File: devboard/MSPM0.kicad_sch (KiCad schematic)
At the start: 24 parts, among them J1 USB_C_USB2.0, SW1 SW, SW2 SW_Push, U1 MSPM0G3507SPMR, U2 AP2112K-3.3, U3 CH340C

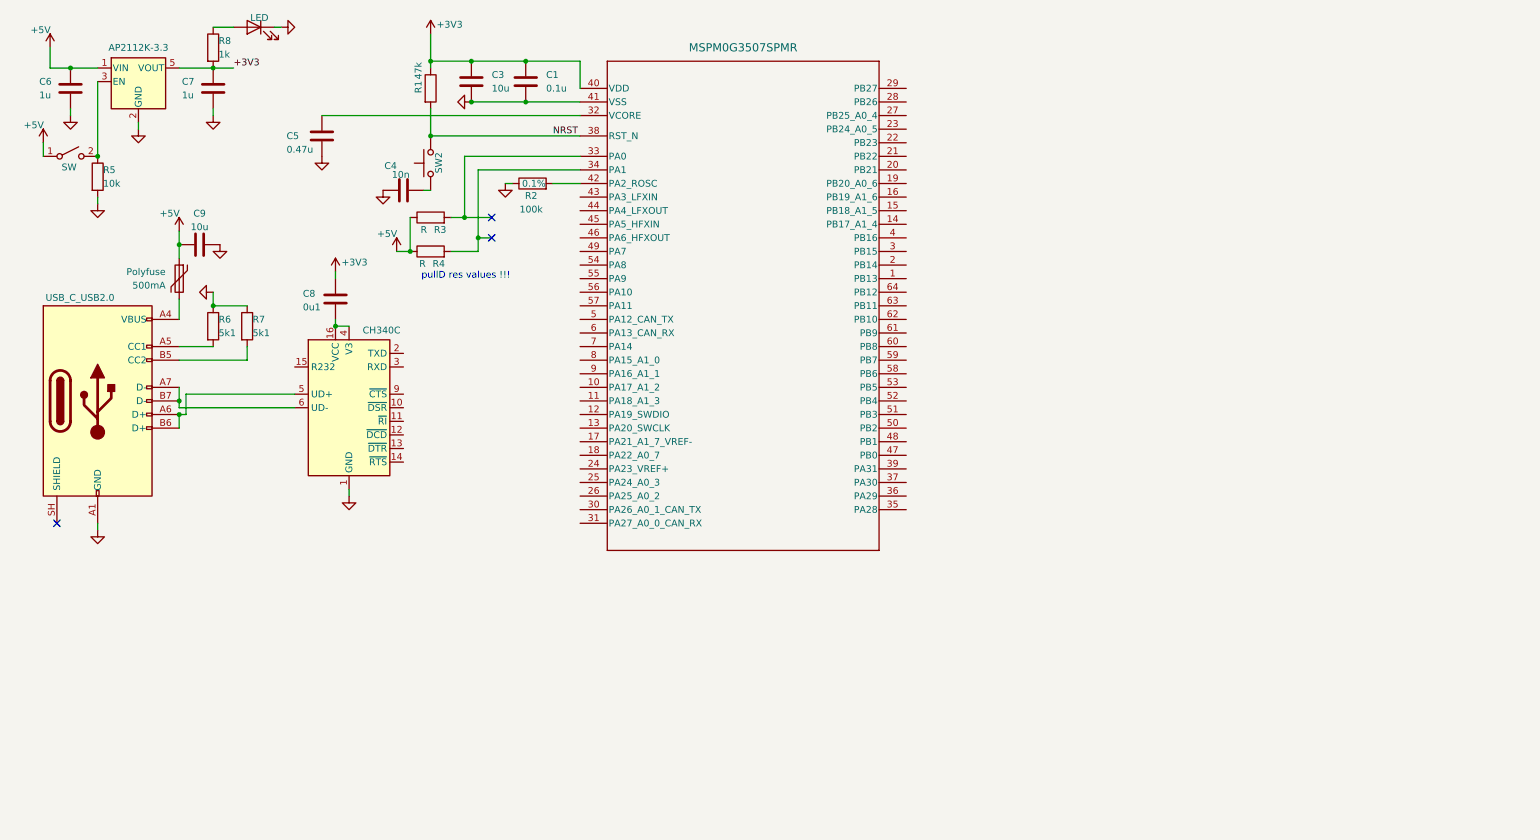
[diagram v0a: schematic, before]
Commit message: added SWD header and configured USB-UART a bit
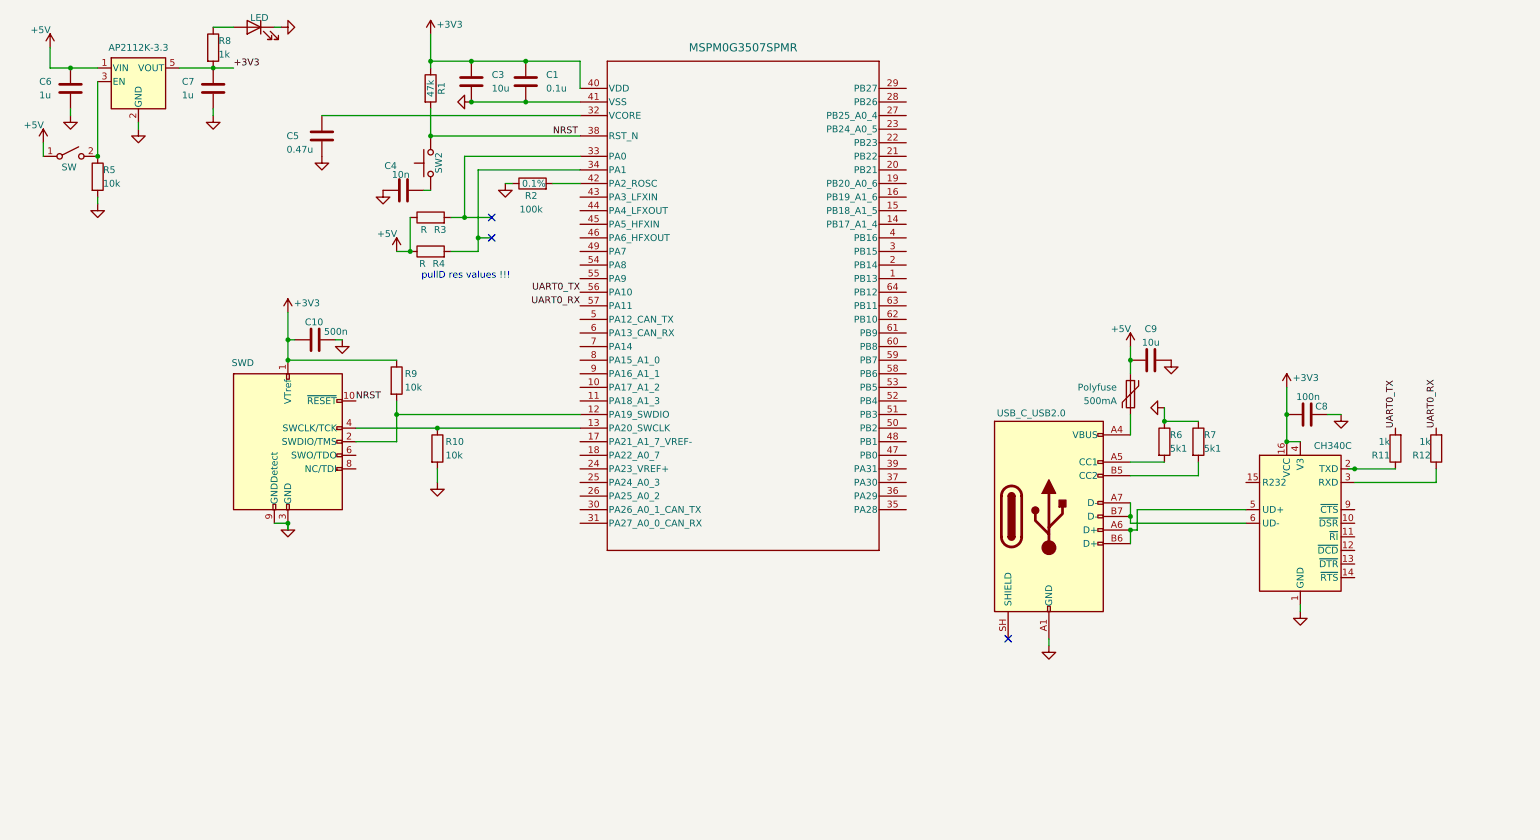
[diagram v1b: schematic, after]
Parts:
- added C10: 500n, symbol Device:C
- added J2: SWD, symbol Connector:Conn_ARM_JTAG_SWD_10
- added R10, R9: 10k, symbol Device:R
- added R11, R12: 1k, symbol Device:R
- C8: value 0u1 -> 100n
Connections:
- net +3V3: now also C8.2, U3.16 (VCC), U3.4 (V3), C10.1, J2.1 (VTref), R9.1; no longer C8.1
- net GND: now also C8.1, C10.2, J2.3 (GND), J2.5 (GND), J2.9 (GNDDetect), R10.2
- net NRST: now also J2.10 (~{RESET})
- net at U1.12 (PA19_SWDIO): now also J2.2 (SWDIO/TMS), R9.2
- net at U1.13 (PA20_SWCLK): now also J2.4 (SWCLK/TCK), R10.1
- net UART0_TX: now reaches U1.56 (PA10)
- net UART0_TX: now also R11.2
- net UART0_RX: now reaches U1.57 (PA11)
- net UART0_RX: now also R12.2
- net at U3.2 (TXD): now also R11.1
- net at U3.3 (RXD): now also R12.1
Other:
- moved on the sheet: C9, Polyfuse, R6, R7

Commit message: gotta start CAN FD
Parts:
- added U4: TCAN1044AVDDFRQ1.A, DDF0008A-IPC_A, symbol TCAN1044AV:TCAN1044AVDDFRQ1.A
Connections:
- net SWO: now reaches U1.8 (PA15_A1_0)
- net SWO: now also J2.6 (SWO/TDO)
- no-connect marks 3 -> 4
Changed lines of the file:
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@@
 		(at 102.87 54.61)
 	)
+	(no_connect
+		(at 77.47 97.79)
+	)
 	(wire
 		(pts
@@
 		)
 	)
+	(label "SWO"
+		(at 119.38 77.47 180)
+		(effects
+			(font
+				(size 1.27 1.27)
+			)
+			(justify right bottom)
+		)
+	)
 	(label "UART0_RX"
 		(at 279.4 90.17 90)
@@
 		)
 	)
+	(label "SWO"
+		(at 77.47 95.25 0)
+		(effects
+			(font
+				(size 1.27 1.27)
+			)
+			(justify left bottom)
+		)
+	)
 	(label "NRST"
 		(at 114.3 35.56 0)
@@
 					(unit 1)
 				)
+			)
+		)
+	)
+	(symbol
+		(lib_id "TCAN1044AV:TCAN1044AVDDFRQ1.A")
+		(at 45.72 134.62 0)
+		(unit 1)
+		(body_style 1)
+		(exclude_from_sim no)
+		(in_bom yes)
+		(on_board yes)
+		(in_pos_files yes)
+		(dnp no)
+		(fields_autoplaced yes)
+		(property "Reference" "U4"
+			(at 66.04 124.46 0)
+			(hide yes)
+			(show_name no)
+			(do_not_autoplace no)
+			(effects
+				(font
+					(size 1.524 1.524)
+				)
+			)
+		)
+		(property "Value" "TCAN1044AVDDFRQ1.A"
+			(at 66.04 127 0)
+			(show_name no)
+			(do_not_autoplace no)
+			(effects
+				(font
+					(size 1.524 1.524)
+				)
+			)
+		)
+		(property "Footprint" "DDF0008A-IPC_A"
+			(at 45.72 134.62 0)
+			(hide yes)
+			(show_name no)
+			(do_not_autoplace no)
+			(effects
+				(font
+					(size 1.27 1.27)
+					(italic yes)
+				)
+			)
+		)
+		(property "Datasheet" "https://www.ti.com/lit/gpn/tcan1044a-q1"
+			(at 45.72 134.62 0)
+			(hide yes)
+			(show_name no)
+			(do_not_autoplace no)
+			(effects
+				(font
+					(size 1.27 1.27)
+					(italic yes)
+				)
+			)
+		)
+		(property "Description" ""
+			(at 45.72 134.62 0)
+			(hide yes)
+			(show_name no)
+			(do_not_autoplace no)
+			(effects
+				(font
+					(size 1.27 1.27)
+				)
+			)
+		)
+		(pin "1"
+		)
+		(pin "4"
+		)
+		(pin "2"
+		)
+		(pin "3"
+		)
+		(pin "6"
+		)
+		(pin "8"
+		)
+		(pin "7"
+		)
+		(pin "5"
+		)
+		(instances
+			(project "MSPM0"
+				(path "/3004d868-29f4-471c-a613-f1fb79301ae2"
+					(reference "U4")
+					(unit 1)
+				)

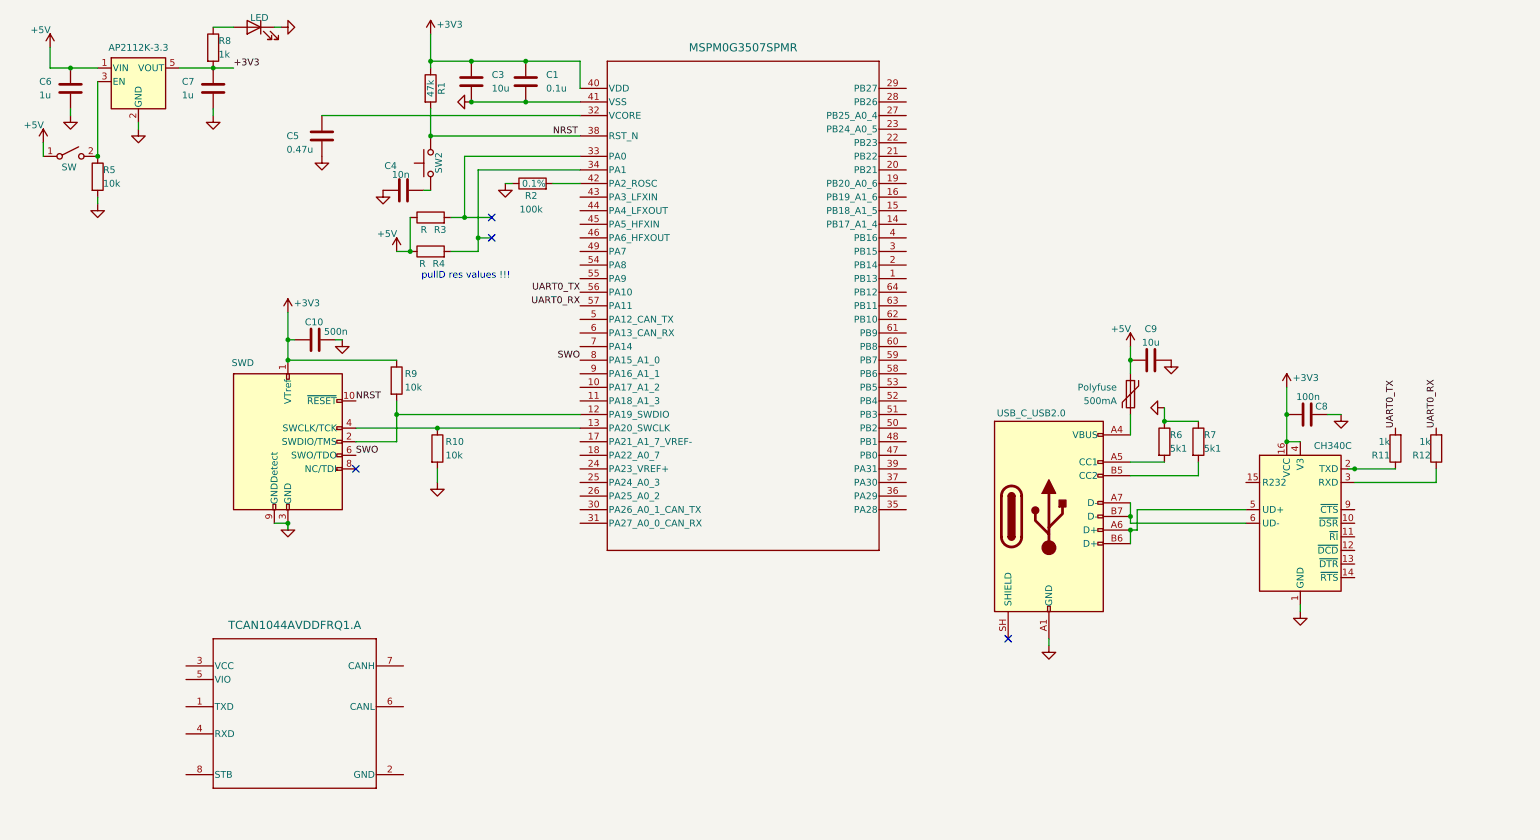
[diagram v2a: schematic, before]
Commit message: 2 LEDs, crystal, and some aesthetics
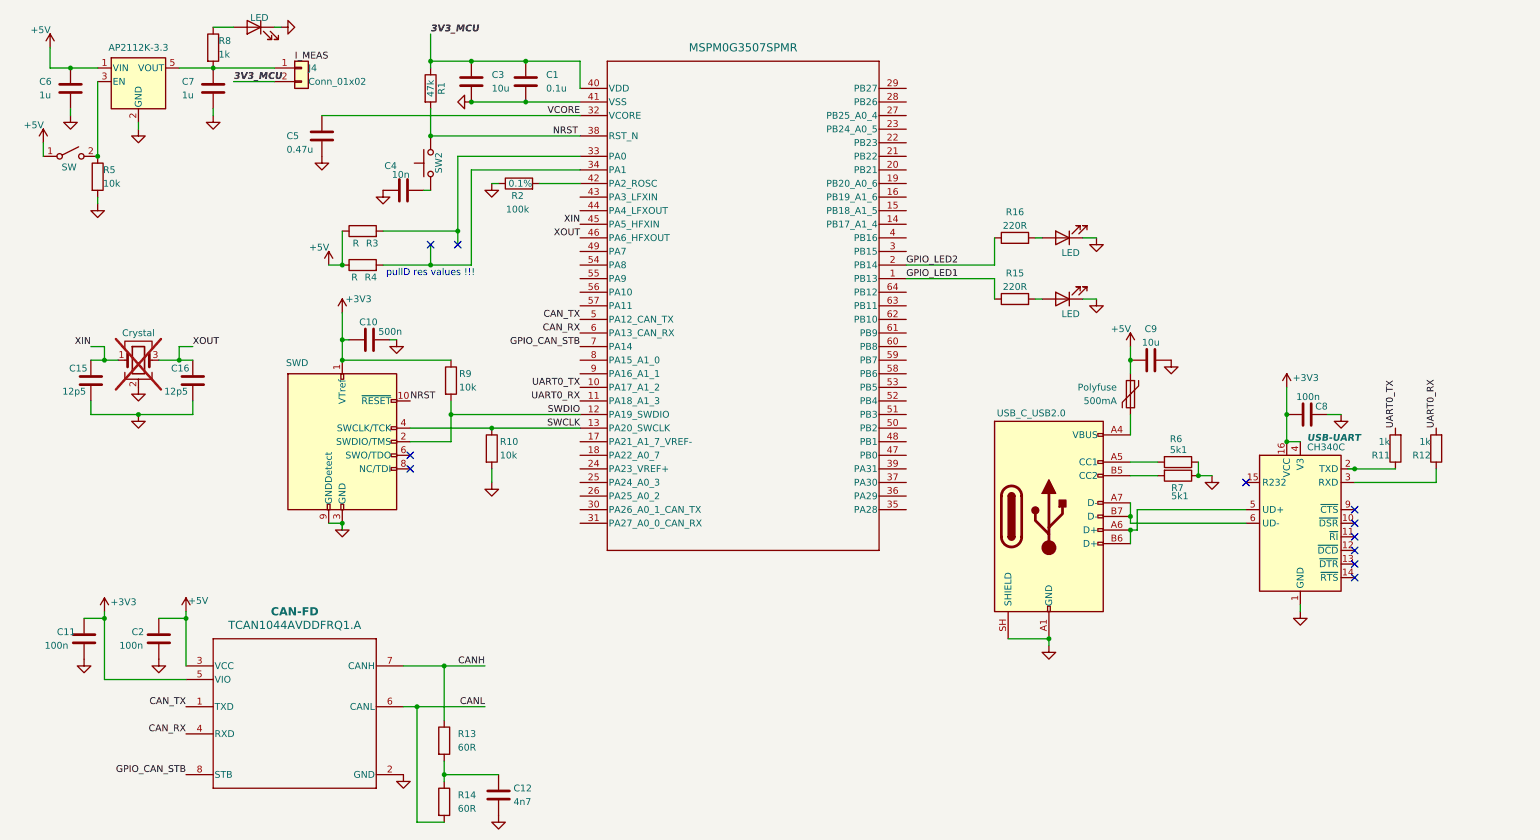
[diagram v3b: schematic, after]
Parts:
- added C11, C2: 100n, symbol Device:C
- added C12: 4n7, symbol Device:C
- added C15, C16: 12p5, symbol Device:C
- added D2, D3: LED, symbol Device:LED
- added J4: Conn_01x02, Connector_PinHeader_2.54mm:PinHeader_1x02_P2.54mm_Vertical, symbol Connector_Generic:Conn_01x02
- added R13, R14: 60R, symbol Device:R
- added R15, R16: 220R, symbol Device:R
- added Y1: Crystal, symbol Device:Crystal_GND24
- renumbered U4 to CAN-FD, U3 to USB-UART
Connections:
- net +3V3: now also CAN-FD.5 (VIO), C11.1; no longer C1.1, C3.1, C7.1, R1.1, R8.2, U1.40 (VDD), U2.5 (VOUT)
- net +5V: now also CAN-FD.3 (VCC), C2.1
- net GND: now also CAN-FD.2 (GND), J1.SH (SHIELD), C11.2, C12.2, C15.2, C16.2, C2.2, D2.1 (K), D3.1 (K), Y1.2 (G), Y1.4 (G)
- net UART0_RX: now also U1.11 (PA18_A1_3); no longer U1.57 (PA11)
- net UART0_TX: now also U1.10 (PA17_A1_2); no longer U1.56 (PA10)
- net SWCLK: now reaches J2.4 (SWCLK/TCK), R10.1, U1.13 (PA20_SWCLK)
- net GPIO_LED1: now reaches U1.1 (PB13)
- net GPIO_LED1: now also R15.1
- net SWDIO: now reaches J2.2 (SWDIO/TMS), R9.2, U1.12 (PA19_SWDIO)
- net GPIO_LED2: now reaches U1.2 (PB14)
- net GPIO_LED2: now also R16.1
- net VCORE: now reaches C5.1, U1.32 (VCORE)
- net XIN: now reaches U1.45 (PA5_HFXIN)
- net XIN: now also C15.1, Y1.1
- net XOUT: now reaches U1.46 (PA6_HFXOUT)
- net XOUT: now also C16.1, Y1.3
- net CAN_TX: now reaches U1.5 (PA12_CAN_TX)
- net CAN_TX: now also CAN-FD.1 (TXD)
- net CAN_RX: now reaches U1.6 (PA13_CAN_RX)
- net CAN_RX: now also CAN-FD.4 (RXD)
- net GPIO_CAN_STB: now reaches U1.7 (PA14)
- net GPIO_CAN_STB: now also CAN-FD.8 (STB)
- net CANL: now reaches CAN-FD.6 (CANL)
- net CANL: now also R14.2
- net CANH: now reaches CAN-FD.7 (CANH)
- net CANH: now also R13.1
- net SWO: no longer names the net of U1.8 (PA15_A1_0)
- net SWO: no longer J2.6 (SWO/TDO)
- new net: C7.1, J4.1 (Pin_1), R8.2, U2.5 (VOUT)
- new net: D2.2 (A), R15.2
- new net: C12.1, R13.2, R14.1
- new net: D3.2 (A), R16.2
- new net 3V3_MCU: C1.1, C3.1, J4.2 (Pin_2), R1.1, U1.40 (VDD)
- no-connect marks 4 -> 11
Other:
- moved on the sheet: C10, R10, R2, R3, R4, R6, R7, R9

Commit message: got rid of ERC errors
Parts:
- removed Y1: Crystal, symbol Device:Crystal_GND24
- added JP1: Jumper_2_Bridged, symbol Jumper:Jumper_2_Bridged
- added R17: 47k, symbol Device:R
- added SW3: SW, symbol Switch:SW_Push
- added TP1: TP_5V, symbol Connector:TestPoint
- added TP2: TP_3V3, symbol Connector:TestPoint
- added Y2: Crystal, Crystal:Crystal_SMD_3225-4Pin_3.2x2.5mm, symbol Device:Crystal_GND24
- C10: value 500n -> 470n
- C15, C16: value 12p5 -> 15p; now not fitted
- CAN-FD1: renamed from CAN-FD; footprint DDF0008A-IPC_A -> TCAN1044AV:DDF0008A-IPC_A
- MCU1: renamed from U1; footprint PM0064A-IPC_A -> MSPM0G3507SPMR (ft):PM0064A-IPC_A
- R13, R14: value 60R -> 62R
- R15, R16: value 220R -> 1k
- R3, R4: value R -> 4k7
- R5, SW1: now not fitted
- R8: value 1k -> 470R
- renumbered Polyfuse to Polyfuse1, USB-UART to USB-UART1
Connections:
- net +3V3: now also C7.1, J4.1 (Pin_1), R3.1, R4.1, R8.2, U2.5 (VOUT), TP2.1
- net +5V: now also C1.2, C10.2, C11.2, C12.2, C15.2, C16.2, C2.2, C3.2, C4.2, C5.2, C6.2, C7.2, C8.1, C9.2, CAN-FD1.2 (GND), D1.1 (K), D2.1 (K), D3.1 (K), J1.A1 (GND), J1.A12 (GND), J1.B1 (GND), J1.B12 (GND), J1.SH (SHIELD), J2.3 (GND), J2.5 (GND), J2.9 (GNDDetect), MCU1.41 (VSS), R10.2, R2.1, R6.1, R7.1, SW2.1, U2.2 (GND), U2.3 (EN), USB-UART1.1 (GND), R17.1, TP1.1, Y2.2 (G), Y2.4 (G); no longer R3.1, R4.1, SW1.1 (A)
- net CANH: now also JP1.1 (A); no longer R13.1
- net NRST: now also C4.1
- net UART0_RX: now also SW3.1
- net XIN: now also Y2.1
- net XOUT: now also Y2.3
- net I2C_SDA: now reaches MCU1.34 (PA1), R4.2
- net at R5.1, SW1.2 (B): no longer U2.3 (EN)
- net I2C_SCL: now reaches MCU1.33 (PA0), R3.2
- removed net GND: C1.2, C10.2, C11.2, C12.2, C15.2, C16.2, C2.2, C3.2, C4.2, C5.2, C6.2, C7.2, C8.1, C9.2, CAN-FD1.2 (GND), D1.1 (K), D2.1 (K), D3.1 (K), J1.A1 (GND), J1.A12 (GND), J1.B1 (GND), J1.B12 (GND), J1.SH (SHIELD), J2.3 (GND), J2.5 (GND), J2.9 (GNDDetect), MCU1.41 (VSS), R10.2, R2.1, R5.2, R6.1, R7.1, U2.2 (GND), USB-UART1.1 (GND)
- new net: R17.2, SW3.2
- new net: JP1.2 (B), R13.1
- no-connect marks 11 -> 57
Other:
- note removed: "pullD res values !!!"
- moved on the sheet: C10, R10, R9

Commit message: started the UNO headers
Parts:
- added J3, J5: Conn_01x03_Pin, symbol Connector:Conn_01x03_Pin
- added R18, R19: 10k, symbol Device:R
- added SW4, SW5: SW_Push, symbol Switch:SW_Push
- added TP3, TP4: TP_GND, symbol Connector:TestPoint
- added TP5: TP_SWDIO, symbol Connector:TestPoint
- added TP6: TP_SWDCLK, symbol Connector:TestPoint
- added TP7: TP_NRST, symbol Connector:TestPoint
- added TP8: TP_UART_RX, symbol Connector:TestPoint
- added TP9: TP_UART_TX, symbol Connector:TestPoint
- C15, C16: now fitted
- MCU1: value MSPM0G3507SPMR -> MSPM0G3507SPMR (LQFP-64)
- Y2: value Crystal -> 40MHz
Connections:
- net +5V: no longer C1.2, C10.2, C11.2, C12.2, C15.2, C16.2, C2.2, C3.2, C4.2, C5.2, C6.2, C7.2, C8.1, C9.2, CAN-FD1.2 (GND), D1.1 (K), D2.1 (K), D3.1 (K), J1.A1 (GND), J1.A12 (GND), J1.B1 (GND), J1.B12 (GND), J1.SH (SHIELD), J2.3 (GND), J2.5 (GND), J2.9 (GNDDetect), MCU1.41 (VSS), R10.2, R17.1, R2.1, R6.1, R7.1, SW2.1, U2.2 (GND), USB-UART1.1 (GND), Y2.2 (G), Y2.4 (G)
- net 3V3_MCU: now also R18.1, R19.1, TP4.1
- net CANH: now also J5.3 (Pin_3)
- net CANL: now also J5.2 (Pin_2)
- net NRST: now also TP7.1
- net SWCLK: now also TP6.1
- net SWDIO: now also TP5.1
- net UART0_RX: now also J3.2 (Pin_2), TP8.1
- net UART0_TX: now also J3.3 (Pin_3), TP9.1
- net PWM_0: now reaches MCU1.17 (PA21_A1_7_VREF-)
- net GPIO_Button1: now reaches MCU1.3 (PB15)
- net GPIO_Button1: now also R18.2, SW4.1
- net GPIO_Button2: now reaches MCU1.4 (PB16)
- net GPIO_Button2: now also R19.2, SW5.1
- net SPI_PICO: now reaches MCU1.55 (PA9)
- net SPI_POCI: now reaches MCU1.56 (PA10)
- net SPI_SCLK: now reaches MCU1.57 (PA11)
- new net GND: C1.2, C10.2, C11.2, C12.2, C15.2, C16.2, C2.2, C3.2, C4.2, C5.2, C6.2, C7.2, C8.1, C9.2, CAN-FD1.2 (GND), D1.1 (K), D2.1 (K), D3.1 (K), J1.A1 (GND), J1.A12 (GND), J1.B1 (GND), J1.B12 (GND), J1.SH (SHIELD), J2.3 (GND), J2.5 (GND), J2.9 (GNDDetect), J3.1 (Pin_1), J5.1 (Pin_1), MCU1.41 (VSS), R10.2, R17.1, R2.1, R6.1, R7.1, SW2.1, SW4.2, SW5.2, TP3.1, U2.2 (GND), USB-UART1.1 (GND), Y2.2 (G), Y2.4 (G)
- no-connect marks 57 -> 51
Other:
- moved on the sheet: R15, R16

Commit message: bro the faah is that pwm doing with ccp0/ccp1 😭
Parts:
- added J6: Conn_01x08_Power, symbol Connector:Conn_01x08_Socket
- added J7: Conn_01x06_Analog, symbol Connector:Conn_01x06_Socket
- added J8: Conn_01x08_DigitalLow, symbol Connector:Conn_01x08_Socket
- added J9: Conn_01x10_DigitalHigh, symbol Connector:Conn_01x10_Socket
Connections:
- net +5V: now also J6.5 (Pin_5)
- net 3V3_MCU: now also J6.4 (Pin_4)
- net GND: now also J6.6 (Pin_6), J6.7 (Pin_7)
- net GPIO_Button1: now also J8.6 (Pin_6)
- net GPIO_Button2: now also J8.7 (Pin_7)
- net GPIO_LED1: now also J8.3 (Pin_3)
- net GPIO_LED2: now also J8.4 (Pin_4)
- net I2C_SCL: now also MCU1.44 (PA4_LFXOUT), R4.2; no longer MCU1.33 (PA0), R3.2
- net I2C_SDA: now also MCU1.43 (PA3_LFXIN), R3.2; no longer MCU1.34 (PA1), R4.2
- net NRST: now also J6.3 (Pin_3)
- net UART0_RX: now also J8.2 (Pin_2)
- net UART0_TX: now also J8.1 (Pin_1)
- net PWM1_CCP1: now reaches MCU1.18 (PA22_A0_7)
- net ADC12_5: now reaches MCU1.23 (PB24_A0_5)
- net ADC12_5: now also J7.6 (Pin_6)
- net ADC12_3: now reaches MCU1.25 (PA24_A0_3)
- net ADC12_3: now also J7.4 (Pin_4)
- net ADC12_2: now reaches MCU1.26 (PA25_A0_2)
- net ADC12_2: now also J7.3 (Pin_3)
- net ADC12_4: now reaches MCU1.27 (PB25_A0_4)
- net ADC12_4: now also J7.5 (Pin_5)
- net ADC12_1: now reaches MCU1.30 (PA26_A0_1_CAN_TX)
- net ADC12_1: now also J7.2 (Pin_2)
- net ADC12_0: now reaches MCU1.31 (PA27_A0_0_CAN_RX)
- net ADC12_0: now also J7.1 (Pin_1)
- net SPI_CS0: now reaches MCU1.54 (PA8)
- net PWM0_CCP0: now reaches MCU1.8 (PA15_A1_0)
- net PWM0_CCP0: now also J8.5 (Pin_5)
- net PWM0_CCP1: now reaches MCU1.9 (PA16_A1_1)
- net PWM_0 renamed PWM1_CCP0
- net PWM1_CCP0: now also J8.8 (Pin_8)
- no-connect marks 51 -> 43
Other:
- note added: "D8, D9 (PWM), D10 (SPI CS, PWM), D11 (MOSI), D12 (MISO), D13 (SCK), GND, AREF, SDA (PA0), SCL (PA1)"
- moved on the sheet: C8, C9, J3, Polyfuse1, R11, R12, R4, R6, R7, USB-UART1
